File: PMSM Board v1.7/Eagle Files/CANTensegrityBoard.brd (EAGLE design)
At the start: 100.5 x 48 mm, 96 parts, among them IC1 DRV8303, U1 TPS73733-Q1_DRB_8, U10 H1206T500R-10, U2 SN65HVD232_D_8, U3 SN65LVDT348_PW_1, U4 TPS54240_DRC_10, U5 LP38692_NGG_6, U6 DSPIC33EP256MU80, U9 H1206T500R-10

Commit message: Finished v1.7
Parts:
- removed SJ1, SJ4, SJ5, SJ6, SJ7: (no value), jumper:SJ
- added JP1: (no value), ASL:2X03
- added LED5, LED6: (no value), ASL:LED-0805
- added R12, R13: 10k, ASL:0805
- added R14, R15: (no value), ASL:0805
- R1: value (none) -> 1 Ohm
- moved U3 50.8 mm to (16.4, 13.1), turned to 90 degrees
- moved U6 48.6 mm to (24.5, 23.9), turned to 180 degrees
- moved SJ8 41.0 mm to (16.2, 30.3), turned to 90 degrees
- moved R17 38.8 mm to (14.0, 30.4), turned to 90 degrees
- moved LED1 26.5 mm to (27.6, 40.3), turned to 90 degrees
- moved LED4 26.2 mm to (23.1, 40.3), turned to 90 degrees
- moved LED2 26.1 mm to (26.1, 40.3), turned to 90 degrees
- moved LED3 26.0 mm to (24.6, 40.3), turned to 90 degrees
- moved C24 22.2 mm to (24.8, 14.1), turned to 270 degrees
- moved U2 20.4 mm to (16.8, 35.3), turned to 180 degrees
- moved C20 19.4 mm to (22.6, 11.9), turned to 270 degrees
- moved C26 19.0 mm to (27.6, 32.7), turned to 90 degrees
- moved U$20 19.0 mm to (3.70, 18.4), turned to 90 degrees
- moved C21 18.5 mm to (23.3, 32.7), turned to 90 degrees
- moved RN1 17.7 mm to (24.2, 36.0), turned to 0 degrees
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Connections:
- removed net EN_A: U3.15
- removed net EN_A+: U3.2
- removed net EN_A-: U3.1
- removed net EN_B: U3.14
- removed net EN_B+: U3.3
- removed net EN_B-: U3.4
- removed net EN_C: U3.11
- removed net EN_C+: U3.6
- removed net EN_C-: U3.5
- removed net N$27: SJ4.2
- removed net N$29: SJ6.2
- removed net N$30: SJ7.2
- removed net N$33: RN1.P$1
- removed net N$41: RN1.P$2
- removed net N$42: RN1.P$3
- removed net N$43: RN1.P$4
- new net CH_A+: U$15.6, U3.6
- new net CH_A-: U$15.5, U3.5
- new net CH_B+: U$15.4, U3.3
- new net CH_B-: U$15.3, U3.4
- new net CH_I+: U$15.2, U3.2
- new net CH_I-: U$15.1, U3.1
- new net EXT1: JP1.1, U6.52
- new net EXT2: JP1.2, U6.51
- new net EXT3: JP1.3, U6.50
- new net HALL1: U$20.3, U6.48
- new net HALL2: U$20.4, U6.47
- new net HALL3: U$20.5, U6.46
- new net LED1: RN1.P$4, U6.21
- new net LED2: RN1.P$3, U6.22
- new net LED3: RN1.P$2, U6.23
- new net LED4: RN1.P$1, U6.24
- new net N$11: LED5.2, R15.2
- new net N$17: LED6.2, R14.2
- new net N$23: R12.2, U$19.P$3
- new net QEI_A: U3.15, U6.55
- new net QEI_B: U3.14, U6.54
- new net QEI_I: U3.11, U6.53
- net *SCS: now also U6.8
- net CANRX: now also U6.31
- net CANTX: now also U6.32
- net CAN_H: now also U$14.P$1, U$19.P$1
- net CAN_L: now also U$14.P$2, U$19.P$2
- net CRNT1: now also U6.27
- net CRNT2: now also U6.28
- net DC_CAL: now also U6.6
- net EN_GATE: now also U6.5
- net GND: now also JP1.4, U$15.7, U$20.2, U6.20, U6.25, U6.41, U6.9
- net MCLR: now also U6.7
- net MISO: now also U6.3
- net MOSI: now also U6.4
- net N$12: now also R14.1
- net N$24: now also R15.1
- net N$25: now also U6.15
- net N$28: now also R13.2, U$14.P$3; no longer SJ5.2
- net N$31: now also U6.56
- net N$5: now also U6.38; no longer SJ1.2
- net PGC: now also U6.18
- net PGD: now also U6.17
- net PGND: now also U$16.1, U$16.4, U$18.2
- net PVDD: now also U$16.2, U$16.3
- net PWM1H: now also U6.1
- net PWM1L: now also U6.64
- net PWM2H: now also U6.63
- net PWM2L: now also U6.62
- net PWM3H: now also U6.61
- net PWM3L: now also U6.60
- net SCLK: now also U6.2
- net SH_A: now also U$17.5, U$17.6
- net SH_B: now also U$17.3, U$17.4
- net SH_C: now also U$17.1, U$17.2
- net VCC3V3: now also JP1.6, LED5.1, LED6.1, U$20.1, U6.10, U6.19, U6.26, U6.57; no longer SJ1.1, SJ4.1, SJ5.1, SJ6.1, SJ7.1
- net VCC5V0: now also JP1.5, U$15.10
- net VCC5V5: now also U$18.1
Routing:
- net VCC3V3: track 17.3 -> 98.5 mm, vias 4 -> 12
- net MCLR: track 0.00 -> 38.0 mm, vias 0 -> 1
- net PWM3L: track 0.00 -> 29.9 mm
- net PWM3H: track 0.00 -> 29.1 mm
- net PGD: track 0.00 -> 28.9 mm, vias 0 -> 1
- net PWM2L: track 0.00 -> 28.2 mm
- net PWM2H: track 0.00 -> 27.4 mm
- net PVDD: track 23.4 -> 50.0 mm
- net CAN_L: track 0.00 -> 25.5 mm
- net PGC: track 0.00 -> 25.4 mm, vias 0 -> 1
- net CRNT2: track 29.5 -> 53.0 mm, vias 1 -> 2
- net CAN_H: track 0.00 -> 22.0 mm
- net CRNT1: track 29.1 -> 49.5 mm, vias 1 -> 2
- net HALL3: track 0.00 -> 16.7 mm
- net DC_CAL: track 16.5 -> 32.7 mm, vias 1 -> 2
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- added copper zone on layer 15, net GND
- added copper zone on layer 2, net GND
- added copper zone on layer 15, net VCC5V0
- added copper zone on layer 15, net VCC5V5
- removed copper zone on layer 15, net VCC3V3
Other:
- board text added: "PMSM Driver v1.7 6-40 V 40 Amps http://pavlo.me (C) - 2013 Pavlo Manovi"
- board text removed: "3.3v"
- board text removed: "Licensed under the TAPR OHL"
- board text removed: "PMSM Driver v1.6 6-40 V 40 Amps http://pavlo.me (C) - 2013 Pavlo Manovi"
- board text removed: "PVDD"
- board text removed: "PWRGD"
- board text removed: "http://www.tapr.org/ohl"

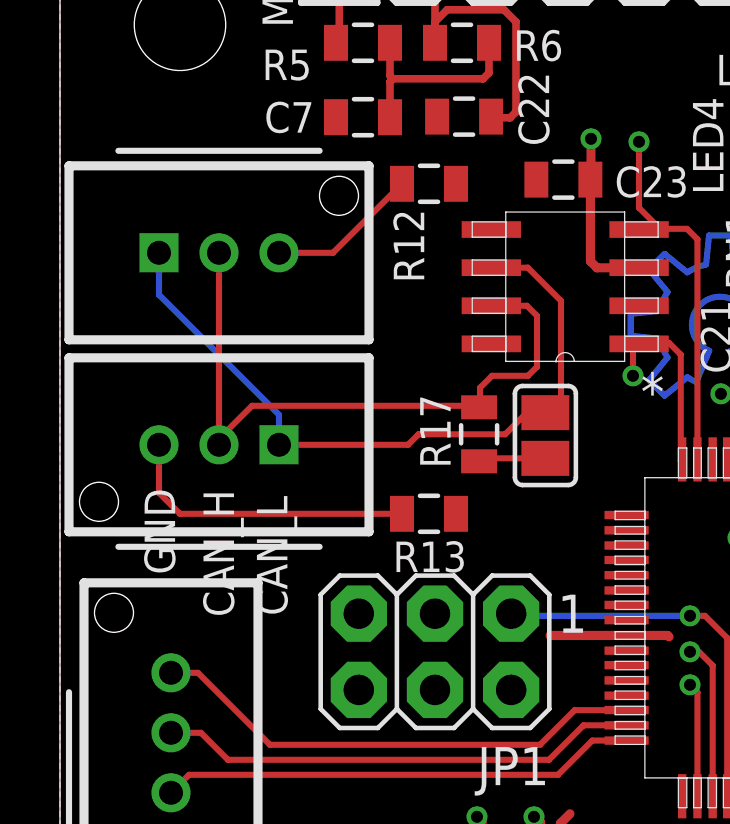
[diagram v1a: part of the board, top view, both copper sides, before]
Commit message: Fixed CAN Connector Pinout
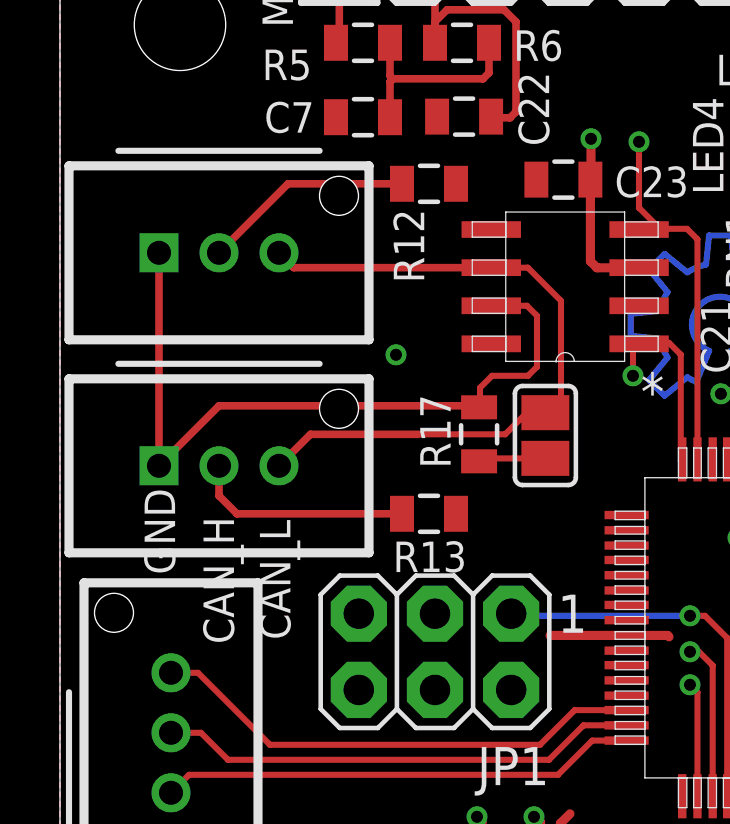
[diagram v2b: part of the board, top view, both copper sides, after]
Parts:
- moved U$14 0.70 mm to (5.30, 29.3), turned to 0 degrees
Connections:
- removed net N$23: R12.2, U$19.P$3
- new net N$27: R12.2, U$19.P$1
- net CAN_H: now also U$14.P$2, U$19.P$2; no longer U$14.P$1, U$19.P$1
- net CAN_L: now also U$14.P$3, U$19.P$3; no longer U$14.P$2, U$19.P$2
- net GND: now also R12.1, R13.1
- net N$28: now also U$14.P$1; no longer U$14.P$3
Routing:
- net N$27: track 0.00 -> 7.05 mm
- net N$23: track 5.05 -> 0.00 mm
- net CAN_H: track 22.0 -> 24.8 mm
- net N$28: track 9.99 -> 7.35 mm
- net GND: vias 29 -> 30
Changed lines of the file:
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@@
 W  V  U</text>
 <text x="27.54" y="46.5" size="1.016" layer="25" rot="R180">ICSP</text>
-<text x="5.8" y="24.26" size="1.016" layer="25" rot="R90">CAN_H</text>
-<text x="7.58" y="24.3" size="1.016" layer="25" rot="R90">CAN_L</text>
+<text x="5.8" y="23.36" size="1.016" layer="25" rot="R90">CAN_H</text>
+<text x="7.68" y="23.5" size="1.016" layer="25" rot="R90">CAN_L</text>
 <text x="91.82" y="47.19" size="1.016" layer="25" rot="R270">V_IN</text>
 <text x="2.82" y="28.55" size="1.016" layer="25" rot="R270">GND</text>
@@
 <attribute name="VALUE" x="43.516" y="47.997" size="0.4064" layer="27" rot="R180"/>
 </element>
-<element name="U$14" library="OpenPMSM" package="55932-0310" value="MICROCLASP3" x="5.3" y="30" smashed="yes" rot="R180"/>
+<element name="U$14" library="OpenPMSM" package="55932-0310" value="MICROCLASP3" x="5.3" y="29.3" smashed="yes"/>
 <element name="U$15" library="OpenPMSM" package="FOUR-WALL-2500-LP-STH" value="3M10PIN2500" x="17.7" y="4.5" smashed="yes"/>
 <element name="U$16" library="OpenPMSM" package="0039288040" value="MINIFITJR4PIN" x="86.5" y="43" smashed="yes"/>
@@
 <contactref element="JP1" pad="4"/>
 <via x="25.2" y="22.7" extent="1-16" drill="0.4" shape="square" alwaysstop="yes"/>
+<contactref element="R12" pad="1"/>
+<contactref element="R13" pad="1"/>
+<via x="11.2" y="33" extent="1-16" drill="0.4" shape="square" alwaysstop="yes"/>
 </signal>
 <signal name="N$2">
@@
 <wire x1="14" y1="31.9" x2="14" y2="31.28" width="0.2032" layer="1"/>
 <wire x1="14" y1="31.28" x2="13.97" y2="31.25" width="0.2032" layer="1"/>
-<contactref element="U$19" pad="P$1"/>
-<contactref element="U$14" pad="P$1"/>
-<wire x1="5.3" y1="36.4" x2="5.3" y2="30" width="0.2032" layer="1"/>
-<wire x1="5.3" y1="30" x2="5.3" y2="30.2" width="0.2032" layer="1"/>
-<wire x1="5.3" y1="30.2" x2="6.4" y2="31.3" width="0.2032" layer="1"/>
-<wire x1="6.4" y1="31.3" x2="13.92" y2="31.3" width="0.2032" layer="1"/>
 <wire x1="13.92" y1="31.3" x2="13.97" y2="31.25" width="0.2032" layer="1"/>
+<contactref element="U$19" pad="P$2"/>
+<contactref element="U$14" pad="P$2"/>
+<wire x1="13.92" y1="31.3" x2="5.3" y2="31.3" width="0.254" layer="1"/>
+<wire x1="5.3" y1="31.3" x2="3.3" y2="29.3" width="0.254" layer="1"/>
+<wire x1="3.3" y1="36.4" x2="3.3" y2="29.3" width="0.254" layer="1"/>
 </signal>
 <signal name="N$64">
@@
 <wire x1="16.7" y1="30.9" x2="16.352" y2="30.9" width="0.2032" layer="1"/>
 <wire x1="16.352" y1="30.9" x2="16.18" y2="31.072" width="0.2032" layer="1"/>
-<contactref element="U$19" pad="P$2"/>
-<contactref element="U$14" pad="P$2"/>
-<wire x1="3.3" y1="36.4" x2="3.3" y2="35" width="0.2032" layer="16"/>
-<wire x1="3.3" y1="35" x2="7.3" y2="31" width="0.2032" layer="16"/>
-<wire x1="7.3" y1="31" x2="7.3" y2="30" width="0.2032" layer="16"/>
-<wire x1="7.3" y1="30" x2="11.6" y2="30" width="0.2032" layer="1"/>
 <wire x1="16.18" y1="31.072" x2="15.562" y2="31.072" width="0.2032" layer="1"/>
 <wire x1="15.562" y1="31.072" x2="14.84" y2="30.35" width="0.2032" layer="1"/>
 <wire x1="14.84" y1="30.35" x2="11.95" y2="30.35" width="0.2032" layer="1"/>
-<wire x1="11.95" y1="30.35" x2="11.6" y2="30" width="0.2032" layer="1"/>
+<contactref element="U$19" pad="P$3"/>
+<contactref element="U$14" pad="P$3"/>
+<wire x1="14.3762" y1="35.905" x2="7.795" y2="35.905" width="0.254" layer="1"/>
+<wire x1="7.795" y1="35.905" x2="7.3" y2="36.4" width="0.254" layer="1"/>
+<wire x1="11.95" y1="30.35" x2="8.35" y2="30.35" width="0.254" layer="1"/>
+<wire x1="8.35" y1="30.35" x2="7.3" y2="29.3" width="0.254" layer="1"/>
 </signal>
 <signal name="N$25">
@@
 <wire x1="18.8866" y1="21.1568" x2="17.1568" y2="21.1568" width="0.2032" layer="1"/>
 </signal>
-<signal name="N$23">
-<contactref element="U$19" pad="P$3"/>
-<contactref element="R12" pad="2"/>
-<wire x1="7.3" y1="36.4" x2="9.1" y2="36.4" width="0.2032" layer="1"/>
-<wire x1="9.1" y1="36.4" x2="11.4" y2="38.7" width="0.2032" layer="1"/>
-</signal>
-<signal name="N$28">
-<contactref element="U$14" pad="P$3"/>
-<contactref element="R13" pad="2"/>
-<wire x1="3.3" y1="30" x2="3.3" y2="28.4" width="0.2032" layer="1"/>
-<wire x1="3.3" y1="28.4" x2="4" y2="27.7" width="0.2032" layer="1"/>
-<wire x1="4" y1="27.7" x2="11.4" y2="27.7" width="0.2032" layer="1"/>
-</signal>
 <signal name="N$11">
 <contactref element="R15" pad="2"/>
@@
 <wire x1="13" y1="24.87" x2="12.5" y2="24.37" width="0.2032" layer="2"/>
 </signal>
+<signal name="N$27">
+<contactref element="U$19" pad="P$1"/>
+<contactref element="R12" pad="2"/>
+<wire x1="11.4" y1="38.7" x2="7.6" y2="38.7" width="0.254" layer="1"/>
+<wire x1="7.6" y1="38.7" x2="5.3" y2="36.4" width="0.254" layer="1"/>
+</signal>
+<signal name="N$28">
+<contactref element="U$14" pad="P$1"/>
+<contactref element="R13" pad="2"/>
+<wire x1="5.3" y1="29.3" x2="5.3" y2="28.3" width="0.254" layer="1"/>
+<wire x1="5.3" y1="28.3" x2="5.9" y2="27.7" width="0.254" layer="1"/>
+<wire x1="5.9" y1="27.7" x2="11.4" y2="27.7" width="0.254" layer="1"/>
+</signal>
 </signals>

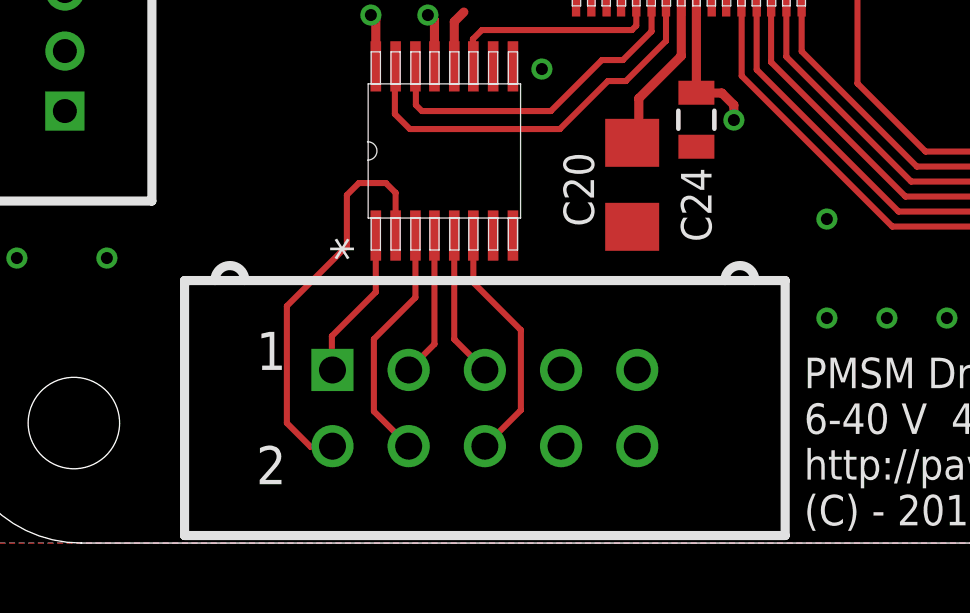
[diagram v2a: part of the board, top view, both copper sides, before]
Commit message: Fixed Optical Encoder Output
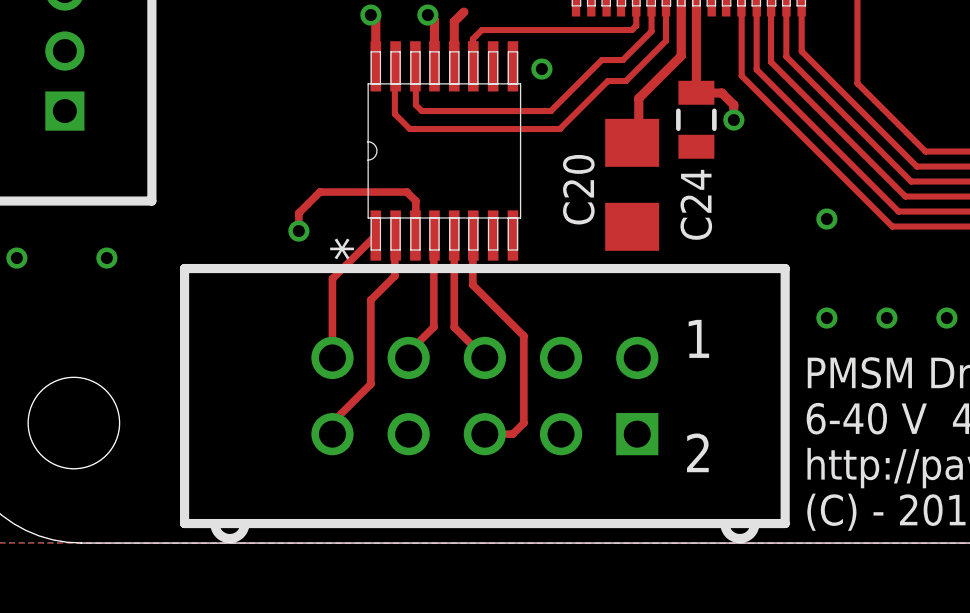
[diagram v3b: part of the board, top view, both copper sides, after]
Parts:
- removed U$15: 3M10PIN2500, OpenPMSM:FOUR-WALL-2500-LP-STH
- added U$21: 3M10PIN2500, OpenPMSM:FOUR-WALL-2500-LP-STH
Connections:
- net CH_A+: now also U$21.6; no longer U$15.6
- net CH_A-: now also U$21.5; no longer U$15.5
- net CH_B+: now also U$21.8; no longer U$15.4
- net CH_B-: now also U$21.7; no longer U$15.3
- net CH_I+: now also U$21.10; no longer U$15.2
- net CH_I-: now also U$21.9; no longer U$15.1
- net GND: now also U$21.3; no longer U$15.7
- net VCC5V0: now also U$21.2; no longer U$15.10
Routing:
- net CH_B+: track 8.07 -> 17.3 mm, vias 0 -> 1
- net CH_I+: track 13.6 -> 7.49 mm
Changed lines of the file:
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@@
 </element>
 <element name="U$14" library="OpenPMSM" package="55932-0310" value="MICROCLASP3" x="5.3" y="29.3" smashed="yes"/>
-<element name="U$15" library="OpenPMSM" package="FOUR-WALL-2500-LP-STH" value="3M10PIN2500" x="17.7" y="4.5" smashed="yes"/>
 <element name="U$16" library="OpenPMSM" package="0039288040" value="MINIFITJR4PIN" x="86.5" y="43" smashed="yes"/>
 <element name="U$17" library="OpenPMSM" package="0039288060" value="MINIFITJR6PIN" x="95.6" y="23.25" smashed="yes" rot="R270"/>
@@
 </element>
 <element name="JP1" library="ASL" package="2X03" value="" x="12.5" y="23.1" rot="R180"/>
+<element name="U$21" library="OpenPMSM" package="FOUR-WALL-2500-LP-STH" value="3M10PIN2500" x="17.7" y="4.9" rot="R180"/>
 </elements>
 <signals>
@@
 <contactref element="U3" pad="9"/>
 <contactref element="U3" pad="12"/>
-<contactref element="U$15" pad="7"/>
 <contactref element="U$20" pad="2"/>
 <via x="2.1" y="9.5" extent="1-16" drill="0.4" shape="square"/>
@@
 <contactref element="R13" pad="1"/>
 <via x="11.2" y="33" extent="1-16" drill="0.4" shape="square" alwaysstop="yes"/>
+<contactref element="U$21" pad="3"/>
 </signal>
 <signal name="N$2">
@@
 <vertex x="0" y="0"/>
 </polygon>
-<contactref element="U$15" pad="10"/>
 <via x="42.3" y="38.2" extent="1-16" drill="0.4" shape="square"/>
 <via x="43.1" y="38.2" extent="1-16" drill="0.4" shape="square"/>
@@
 <wire x1="43.3" y1="38.4" x2="43.1" y2="38.2" width="0.4064" layer="1"/>
 <contactref element="JP1" pad="5"/>
+<contactref element="U$21" pad="2"/>
 </signal>
 <signal name="LED4">
@@
 </signal>
 <signal name="CH_A+">
-<contactref element="U$15" pad="6"/>
 <contactref element="U3" pad="6"/>
-<wire x1="17.3152" y1="10.2506" x2="17.3152" y2="8.6848" width="0.2032" layer="1"/>
-<wire x1="17.3152" y1="8.6848" x2="18.9" y2="7.1" width="0.2032" layer="1"/>
-<wire x1="18.9" y1="7.1" x2="18.9" y2="4.43" width="0.2032" layer="1"/>
-<wire x1="18.9" y1="4.43" x2="17.7" y2="3.23" width="0.2032" layer="1"/>
+<contactref element="U$21" pad="6"/>
+<wire x1="17.7" y1="3.63" x2="18.63" y2="3.63" width="0.254" layer="1"/>
+<wire x1="18.63" y1="3.63" x2="19" y2="4" width="0.254" layer="1"/>
+<wire x1="19" y1="4" x2="19" y2="6.9" width="0.254" layer="1"/>
+<wire x1="19" y1="6.9" x2="17.3" y2="8.6" width="0.254" layer="1"/>
+<wire x1="17.3" y1="8.6" x2="17.3" y2="10.2354" width="0.254" layer="1"/>
+<wire x1="17.3" y1="10.2354" x2="17.3152" y2="10.2506" width="0.254" layer="1"/>
 </signal>
 <signal name="CH_A-">
-<contactref element="U$15" pad="5"/>
 <contactref element="U3" pad="5"/>
-<wire x1="16.6802" y1="10.2506" x2="16.6802" y2="6.7898" width="0.2032" layer="1"/>
-<wire x1="16.6802" y1="6.7898" x2="17.7" y2="5.77" width="0.2032" layer="1"/>
+<contactref element="U$21" pad="5"/>
+<wire x1="16.6802" y1="10.2506" x2="16.6802" y2="7.1898" width="0.254" layer="1"/>
+<wire x1="16.6802" y1="7.1898" x2="17.7" y2="6.17" width="0.254" layer="1"/>
 </signal>
 <signal name="CH_B+">
-<contactref element="U$15" pad="4"/>
 <contactref element="U3" pad="3"/>
-<wire x1="15.3848" y1="10.2506" x2="15.3848" y2="8.1848" width="0.2032" layer="1"/>
-<wire x1="15.3848" y1="8.1848" x2="14" y2="6.8" width="0.2032" layer="1"/>
-<wire x1="14" y1="6.8" x2="14" y2="4.39" width="0.2032" layer="1"/>
-<wire x1="14" y1="4.39" x2="15.16" y2="3.23" width="0.2032" layer="1"/>
+<contactref element="U$21" pad="8"/>
+<wire x1="15.16" y1="3.63" x2="15.16" y2="4.16" width="0.254" layer="2"/>
+<wire x1="15.16" y1="4.16" x2="16.4" y2="5.4" width="0.254" layer="2"/>
+<wire x1="16.4" y1="5.4" x2="16.4" y2="8.7" width="0.254" layer="2"/>
+<wire x1="16.4" y1="8.7" x2="14.7" y2="10.4" width="0.254" layer="2"/>
+<wire x1="14.7" y1="10.4" x2="11.5" y2="10.4" width="0.254" layer="2"/>
+<via x="11.5" y="10.4" extent="1-16" drill="0.4" shape="square"/>
+<wire x1="11.5" y1="10.4" x2="11.5" y2="11" width="0.254" layer="1"/>
+<wire x1="11.5" y1="11" x2="12.2" y2="11.7" width="0.254" layer="1"/>
+<wire x1="12.2" y1="11.7" x2="15.1" y2="11.7" width="0.254" layer="1"/>
+<wire x1="15.1" y1="11.7" x2="15.4" y2="11.4" width="0.254" layer="1"/>
+<wire x1="15.4" y1="11.4" x2="15.4" y2="10.2658" width="0.254" layer="1"/>
+<wire x1="15.4" y1="10.2658" x2="15.3848" y2="10.2506" width="0.254" layer="1"/>
 </signal>
 <signal name="CH_B-">
-<contactref element="U$15" pad="3"/>
 <contactref element="U3" pad="4"/>
-<wire x1="16.0198" y1="10.2506" x2="16.0198" y2="6.6298" width="0.2032" layer="1"/>
-<wire x1="16.0198" y1="6.6298" x2="15.16" y2="5.77" width="0.2032" layer="1"/>
+<contactref element="U$21" pad="7"/>
+<wire x1="15.16" y1="6.17" x2="15.16" y2="6.36" width="0.254" layer="1"/>
+<wire x1="15.16" y1="6.36" x2="16" y2="7.2" width="0.254" layer="1"/>
+<wire x1="16" y1="7.2" x2="16" y2="10.2308" width="0.254" layer="1"/>
+<wire x1="16" y1="10.2308" x2="16.0198" y2="10.2506" width="0.254" layer="1"/>
 </signal>
 <signal name="CH_I+">
-<contactref element="U$15" pad="2"/>
 <contactref element="U3" pad="2"/>
-<wire x1="14.7244" y1="10.2506" x2="14.7244" y2="11.6756" width="0.2032" layer="1"/>
-<wire x1="14.7244" y1="11.6756" x2="14.4" y2="12" width="0.2032" layer="1"/>
-<wire x1="14.4" y1="12" x2="13.5" y2="12" width="0.2032" layer="1"/>
-<wire x1="13.5" y1="12" x2="13.1" y2="11.6" width="0.2032" layer="1"/>
-<wire x1="13.1" y1="11.6" x2="13.1" y2="9.9" width="0.2032" layer="1"/>
-<wire x1="13.1" y1="9.9" x2="11.1" y2="7.9" width="0.2032" layer="1"/>
-<wire x1="11.1" y1="7.9" x2="11.1" y2="4" width="0.2032" layer="1"/>
-<wire x1="11.1" y1="4" x2="11.9" y2="3.2" width="0.2032" layer="1"/>
-<wire x1="11.9" y1="3.2" x2="12.59" y2="3.2" width="0.2032" layer="1"/>
-<wire x1="12.59" y1="3.2" x2="12.62" y2="3.23" width="0.2032" layer="1"/>
+<contactref element="U$21" pad="10"/>
+<wire x1="12.62" y1="3.63" x2="12.62" y2="4.02" width="0.254" layer="1"/>
+<wire x1="12.62" y1="4.02" x2="13.9" y2="5.3" width="0.254" layer="1"/>
+<wire x1="13.9" y1="5.3" x2="13.9" y2="8.1" width="0.254" layer="1"/>
+<wire x1="13.9" y1="8.1" x2="14.7" y2="8.9" width="0.254" layer="1"/>
+<wire x1="14.7" y1="8.9" x2="14.7" y2="10.2262" width="0.254" layer="1"/>
+<wire x1="14.7" y1="10.2262" x2="14.7244" y2="10.2506" width="0.254" layer="1"/>
 </signal>
 <signal name="CH_I-">
-<contactref element="U$15" pad="1"/>
 <contactref element="U3" pad="1"/>
-<wire x1="14.064" y1="10.2506" x2="14.064" y2="8.364" width="0.2032" layer="1"/>
-<wire x1="14.064" y1="8.364" x2="12.6" y2="6.9" width="0.2032" layer="1"/>
-<wire x1="12.6" y1="6.9" x2="12.6" y2="5.79" width="0.2032" layer="1"/>
-<wire x1="12.6" y1="5.79" x2="12.62" y2="5.77" width="0.2032" layer="1"/>
+<contactref element="U$21" pad="9"/>
+<wire x1="12.62" y1="6.17" x2="12.62" y2="8.8066" width="0.254" layer="1"/>
+<wire x1="12.62" y1="8.8066" x2="14.064" y2="10.2506" width="0.254" layer="1"/>
 </signal>
 <signal name="HALL1">
